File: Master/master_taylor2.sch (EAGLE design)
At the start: 43 parts, among them J1 ISP, K1 653002114822, K2 653002114822, K3 653002114822, K4 653002114822, U1 ATMEGA128RFA1, U2 TPS73633-DBVT, U3 ULN2003ADR, Y1 16MHz

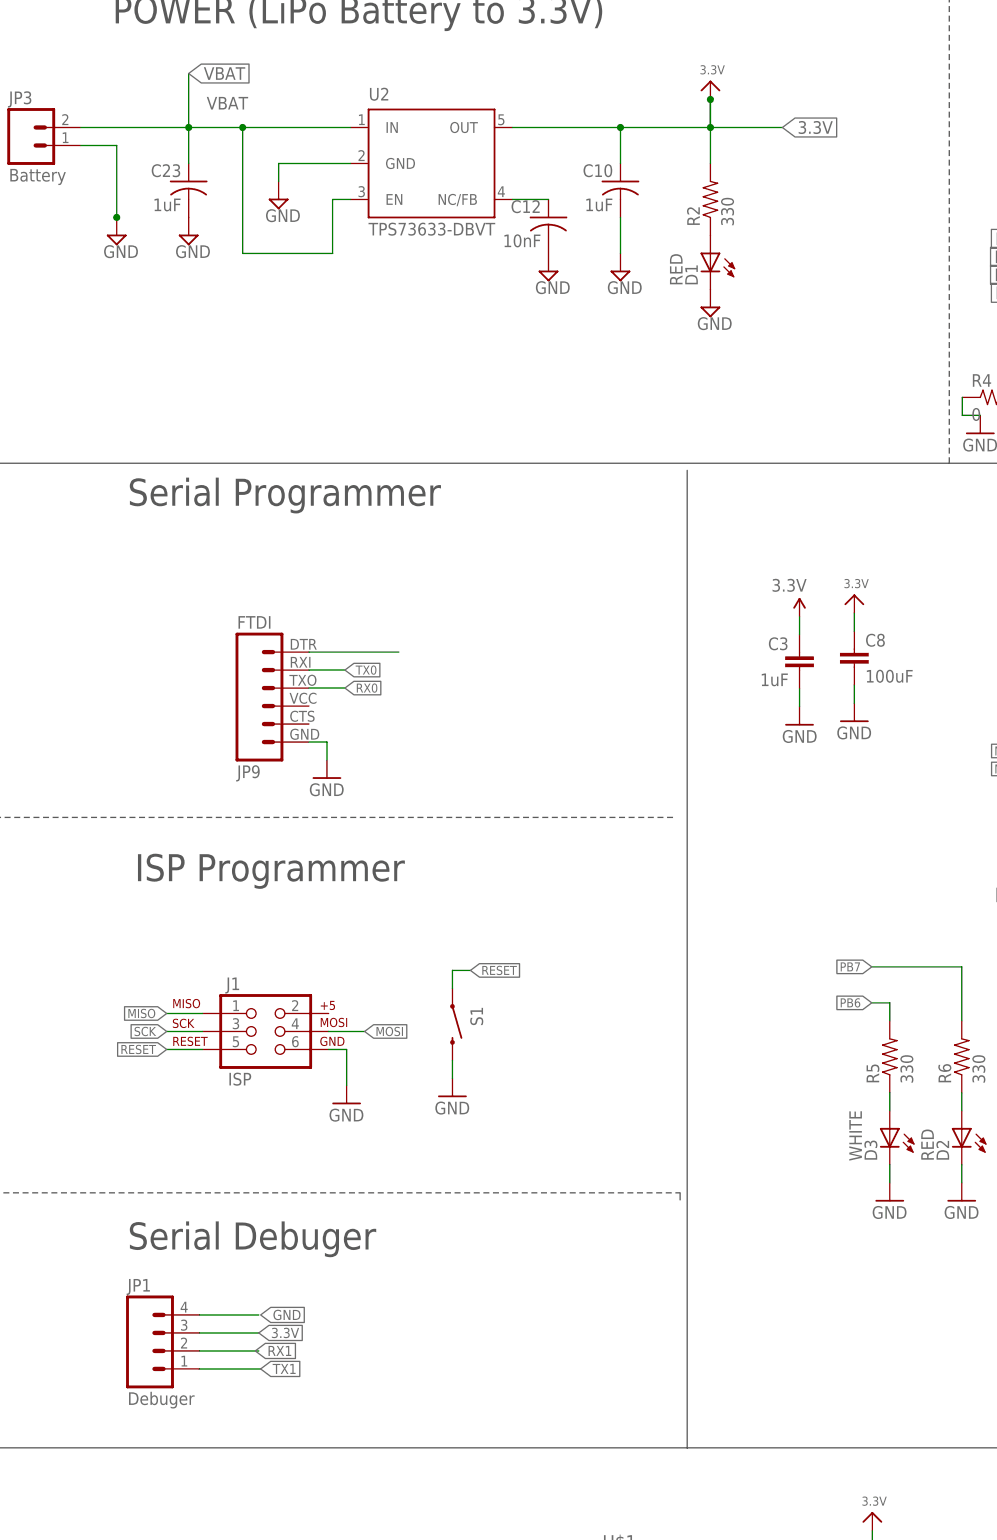
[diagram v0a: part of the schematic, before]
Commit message: Version 2 routed
Layed out crystal and antenna in accordance with the Cult of Sparkfun
Added keepouts to IMU because of Jorge's recommendation
Added keepout to antenna to not disturb the ether wind.
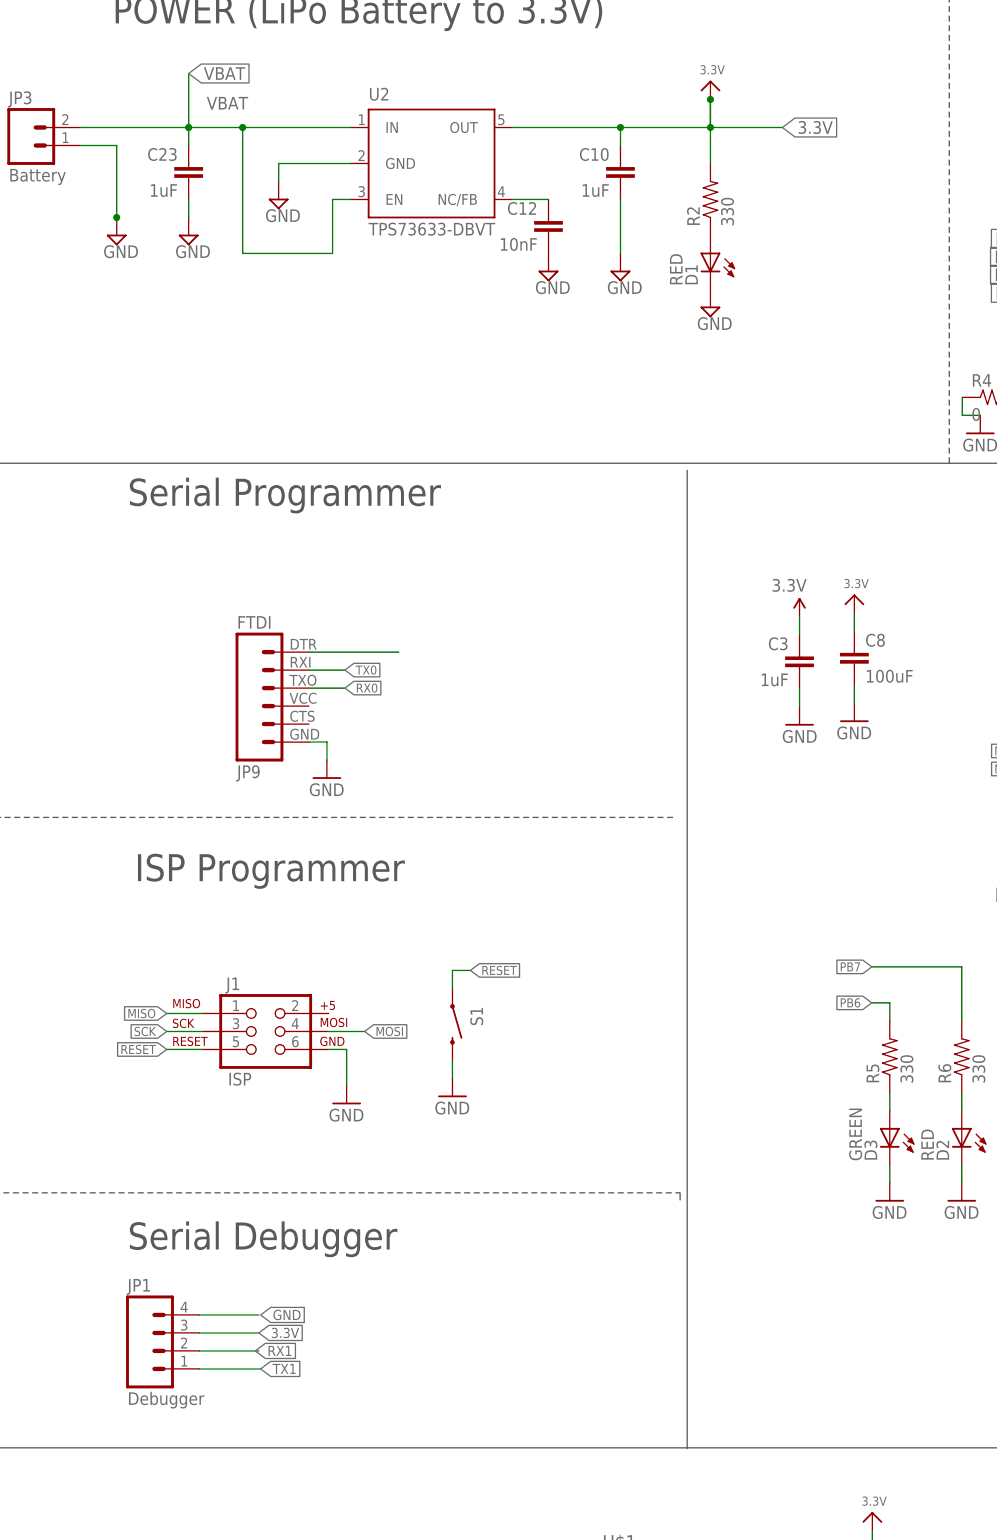
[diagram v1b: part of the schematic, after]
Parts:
- C10, C12, C23: device resistor:C-USC0805 -> SparkFun-Capacitors:CAP0603-CAP
- D3: value WHITE -> GREEN
- JP1: value Debuger -> Debugger
- U1: device SparkFun-DigitalIC:ATMEGA128RFA1 -> master_devon:ATMEGA128RFA1
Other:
- note added: "Serial Debugger"
- note removed: "Serial Debuger"
- moved on the sheet: C10, C23
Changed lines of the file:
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@@
 </classes>
 <parts>
-<part name="U1" library="SparkFun-DigitalIC" deviceset="ATMEGA128RFA1" device=""/>
+<part name="U1" library="master_devon" deviceset="ATMEGA128RFA1" device=""/>
 <part name="GND1" library="SparkFun-Aesthetics" deviceset="GND" device=""/>
 <part name="C1" library="SparkFun-Capacitors" deviceset="CAP" device="0603-CAP" value="1uF"/>
@@
 <part name="C6" library="SparkFun-Capacitors" deviceset="CAP" device="0603-CAP" value="12pF"/>
 <part name="GND6" library="SparkFun-Aesthetics" deviceset="GND" device=""/>
-<part name="GND7" library="SparkFun-Aesthetics" deviceset="GND" device=""/>
+<part name="GND7INF" library="SparkFun-Aesthetics" deviceset="GND" device=""/>
 <part name="B1" library="SparkFun-RF" deviceset="BALUN" device="0805" value="748421245"/>
 <part name="C11" library="SparkFun-Capacitors" deviceset="CAP" device="0603-CAP" value="22pF"/>
@@
 <part name="C16" library="SparkFun-Capacitors" deviceset="CAP" device="0603-CAP" value="JUMP"/>
 <part name="C17" library="SparkFun-Capacitors" deviceset="CAP" device="0603-CAP" value="JUMP"/>
-<part name="D3" library="led" deviceset="LED" device="CHIPLED_0603" value="WHITE"/>
+<part name="D3" library="led" deviceset="LED" device="CHIPLED_0603" value="GREEN"/>
 <part name="R5" library="SparkFun-Resistors" deviceset="RESISTOR" device="0603-RES" value="330"/>
 <part name="R6" library="SparkFun-Resistors" deviceset="RESISTOR" device="0603-RES" value="330"/>
@@
 <part name="SUPPLY8" library="supply2" deviceset="GND" device=""/>
 <part name="U2" library="Power" deviceset="TPS73633-DBVT" device=""/>
-<part name="C10" library="resistor" deviceset="C-US" device="C0805" value="1uF"/>
+<part name="C10" library="SparkFun-Capacitors" deviceset="CAP" device="0603-CAP" value="1uF"/>
 <part name="SUPPLY2" library="supply2" deviceset="GND" device=""/>
-<part name="C12" library="resistor" deviceset="C-US" device="C0805" value="10nF"/>
-<part name="C23" library="resistor" deviceset="C-US" device="C0805" value="1uF"/>
+<part name="C12" library="SparkFun-Capacitors" deviceset="CAP" device="0603-CAP" value="10nF"/>
+<part name="C23" library="SparkFun-Capacitors" deviceset="CAP" device="0603-CAP" value="1uF"/>
 <part name="SUPPLY3" library="supply2" deviceset="GND" device=""/>
 <part name="R2" library="SparkFun-Resistors" deviceset="RESISTOR" device="0603-RES" value="330"/>
@@
 <part name="SUPPLY4" library="supply2" deviceset="GND" device=""/>
 <part name="FRAME1" library="frames" deviceset="FRAME_B_L" device="" value="NONE"/>
-<part name="JP1" library="SparkFun-Connectors" deviceset="M04" device="PTH" value="Debuger"/>
+<part name="JP1" library="SparkFun-Connectors" deviceset="M04" device="PTH" value="Debugger"/>
 <part name="U$2" library="microbuilder" deviceset="3.3V" device=""/>
 <part name="U$1" library="IMU_parts" deviceset="LSM9DS0" device=""/>
@@
 <text x="-255" y="226" size="3.81" layer="97">Serial Programmer</text>
 <text x="-254" y="173" size="3.81" layer="97">ISP Programmer</text>
-<text x="-255" y="121" size="3.81" layer="97">Serial Debuger</text>
+<text x="-255" y="121" size="3.81" layer="97">Serial Debugger</text>
 <text x="-123" y="220" size="3.81" layer="97">ATMEL RF Microcontroller </text>
 <wire x1="38.354" y1="66.294" x2="38.354" y2="232.156" width="0.1524" layer="97"/>
@@
 </instance>
 <instance part="GND6" gate="1" x="-40.72" y="138.04" rot="MR0"/>
-<instance part="GND7" gate="1" x="-50.88" y="138.04" rot="MR0"/>
+<instance part="GND7INF" gate="1" x="-50.88" y="138.04" rot="MR0"/>
 <instance part="B1" gate="G$1" x="-15.32" y="183.76" smashed="yes" rot="MR0">
 <attribute name="VALUE" x="-10.24" y="174.108" size="1.778" layer="96" rot="MR90"/>
@@
 <instance part="C10" gate="G$1" x="-185.42" y="271.78" rot="MR0"/>
 <instance part="SUPPLY2" gate="GND" x="-185.42" y="259.08"/>
-<instance part="C12" gate="G$1" x="-195.58" y="266.7" rot="MR0"/>
+<instance part="C12" gate="G$1" x="-195.58" y="264.16" rot="MR0"/>
 <instance part="C23" gate="G$1" x="-246.38" y="271.78" rot="MR0"/>
 <instance part="SUPPLY3" gate="GND" x="-233.68" y="269.24"/>
@@
 <segment>
 <pinref part="C6" gate="G$1" pin="2"/>
-<pinref part="GND7" gate="1" pin="GND"/>
+<pinref part="GND7INF" gate="1" pin="GND"/>
 <wire x1="-50.88" y1="140.58" x2="-50.88" y2="143.12" width="0.1524" layer="91"/>
 </segment>
@@
 <pinref part="C10" gate="G$1" pin="2"/>
 <pinref part="SUPPLY2" gate="GND" pin="GND"/>
-<wire x1="-185.42" y1="266.7" x2="-185.42" y2="261.62" width="0.1524" layer="91"/>
+<wire x1="-185.42" y1="269.24" x2="-185.42" y2="261.62" width="0.1524" layer="91"/>
 </segment>
 <segment>
@@
 <pinref part="SUPPLY8" gate="GND" pin="GND"/>
 <pinref part="C23" gate="G$1" pin="2"/>
+<wire x1="-246.38" y1="266.7" x2="-246.38" y2="269.24" width="0.1524" layer="91"/>
 </segment>
 <segment>
@@
 <wire x1="-200.66" y1="279.4" x2="-185.42" y2="279.4" width="0.1524" layer="91"/>
 <pinref part="C10" gate="G$1" pin="1"/>
-<wire x1="-185.42" y1="274.32" x2="-185.42" y2="279.4" width="0.1524" layer="91"/>
+<wire x1="-185.42" y1="276.86" x2="-185.42" y2="279.4" width="0.1524" layer="91"/>
 <wire x1="-185.42" y1="279.4" x2="-172.72" y2="279.4" width="0.1524" layer="91"/>
 <label x="-162.56" y="279.4" size="1.778" layer="95" xref="yes"/>
@@
 <wire x1="-261.62" y1="279.4" x2="-246.38" y2="279.4" width="0.1524" layer="91"/>
 <pinref part="C23" gate="G$1" pin="1"/>
-<wire x1="-246.38" y1="274.32" x2="-246.38" y2="279.4" width="0.1524" layer="91"/>
+<wire x1="-246.38" y1="276.86" x2="-246.38" y2="279.4" width="0.1524" layer="91"/>
 <junction x="-246.38" y="279.4"/>
 <wire x1="-246.38" y1="279.4" x2="-238.76" y2="279.4" width="0.1524" layer="91"/>
@@
 </sheet>
 </sheets>
-<errors>
-</errors>
 </schematic>
 </drawing>

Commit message: ng
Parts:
- renumbered K1 to WING_BL, K2 to WING_BR, K3 to WING_FL, K4 to WING_FR
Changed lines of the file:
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@@
 <part name="GND31" library="SparkFun" deviceset="GND" device=""/>
 <part name="A1" library="SparkFun-RF" deviceset="ANTENNA2" device="SMD5"/>
-<part name="K1" library="Wuerth_Elektronik_eiCan_Wire_to_Board_Connectors" deviceset="653002114822" device="">
+<part name="WING_BL" library="Wuerth_Elektronik_eiCan_Wire_to_Board_Connectors" deviceset="653002114822" device="">
 <attribute name="MF" value=""/>
 <attribute name="MPN" value=""/>
 <attribute name="OC_FARNELL" value="unknown"/>
 </part>
-<part name="K2" library="Wuerth_Elektronik_eiCan_Wire_to_Board_Connectors" deviceset="653002114822" device="">
+<part name="WING_BR" library="Wuerth_Elektronik_eiCan_Wire_to_Board_Connectors" deviceset="653002114822" device="">
 <attribute name="MF" value=""/>
 <attribute name="MPN" value=""/>
 <attribute name="OC_FARNELL" value="unknown"/>
 </part>
-<part name="K3" library="Wuerth_Elektronik_eiCan_Wire_to_Board_Connectors" deviceset="653002114822" device="">
+<part name="WING_FL" library="Wuerth_Elektronik_eiCan_Wire_to_Board_Connectors" deviceset="653002114822" device="">
 <attribute name="MF" value=""/>
 <attribute name="MPN" value=""/>
 <attribute name="OC_FARNELL" value="unknown"/>
 </part>
-<part name="K4" library="Wuerth_Elektronik_eiCan_Wire_to_Board_Connectors" deviceset="653002114822" device="">
+<part name="WING_FR" library="Wuerth_Elektronik_eiCan_Wire_to_Board_Connectors" deviceset="653002114822" device="">
 <attribute name="MF" value=""/>
 <attribute name="MPN" value=""/>
@@
 <instance part="GND31" gate="1" x="-137.24" y="127.88"/>
 <instance part="A1" gate="G$1" x="2.46" y="199"/>
-<instance part="K1" gate="G$1" x="-88.18" y="275.16" rot="R90">
+<instance part="WING_BL" gate="G$1" x="-88.18" y="275.16" rot="R90">
 <attribute name="OC_FARNELL" x="-88.18" y="275.16" size="1.778" layer="96" display="off"/>
 <attribute name="MF" x="-88.18" y="275.16" size="1.778" layer="96" display="off"/>
 <attribute name="MPN" x="-88.18" y="275.16" size="1.778" layer="96" display="off"/>
 </instance>
-<instance part="K2" gate="G$1" x="-62.78" y="275.16" rot="R90">
+<instance part="WING_BR" gate="G$1" x="-62.78" y="275.16" rot="R90">
 <attribute name="OC_FARNELL" x="-62.78" y="275.16" size="1.778" layer="96" display="off"/>
 <attribute name="MF" x="-62.78" y="275.16" size="1.778" layer="96" display="off"/>
 <attribute name="MPN" x="-62.78" y="275.16" size="1.778" layer="96" display="off"/>
 </instance>
-<instance part="K3" gate="G$1" x="-37.38" y="275.16" rot="R90">
+<instance part="WING_FL" gate="G$1" x="-37.38" y="275.16" rot="R90">
 <attribute name="OC_FARNELL" x="-37.38" y="275.16" size="1.778" layer="96" display="off"/>
 <attribute name="MF" x="-37.38" y="275.16" size="1.778" layer="96" display="off"/>
 <attribute name="MPN" x="-37.38" y="275.16" size="1.778" layer="96" display="off"/>
 </instance>
-<instance part="K4" gate="G$1" x="-11.98" y="275.16" rot="R90">
+<instance part="WING_FR" gate="G$1" x="-11.98" y="275.16" rot="R90">
 <attribute name="OC_FARNELL" x="-11.98" y="275.16" size="1.778" layer="96" display="off"/>
 <attribute name="MF" x="-11.98" y="275.16" size="1.778" layer="96" display="off"/>
@@
 <wire x1="-88.9" y1="264.16" x2="-75.48" y2="263.68" width="0.1524" layer="91"/>
 <wire x1="-75.48" y1="263.68" x2="-75.48" y2="272.62" width="0.1524" layer="91"/>
-<pinref part="K1" gate="G$1" pin="2"/>
+<pinref part="WING_BL" gate="G$1" pin="2"/>
 <wire x1="-75.48" y1="272.62" x2="-80.56" y2="272.62" width="0.1524" layer="91"/>
 </segment>
@@
 <segment>
 <pinref part="U3" gate="A" pin="2C"/>
-<pinref part="K2" gate="G$1" pin="2"/>
+<pinref part="WING_BR" gate="G$1" pin="2"/>
 <wire x1="-88.9" y1="261.62" x2="-55.16" y2="261.14" width="0.1524" layer="91"/>
 <wire x1="-55.16" y1="261.14" x2="-55.16" y2="272.62" width="0.1524" layer="91"/>
@@
 <wire x1="-88.9" y1="259.08" x2="-27.22" y2="258.6" width="0.1524" layer="91"/>
 <wire x1="-27.22" y1="258.6" x2="-27.22" y2="272.62" width="0.1524" layer="91"/>
-<pinref part="K3" gate="G$1" pin="2"/>
+<pinref part="WING_FL" gate="G$1" pin="2"/>
 <wire x1="-27.22" y1="272.62" x2="-29.76" y2="272.62" width="0.1524" layer="91"/>
 </segment>
@@
 <wire x1="-88.9" y1="256.54" x2="-1.82" y2="256.06" width="0.1524" layer="91"/>
 <wire x1="-1.82" y1="256.06" x2="-1.82" y2="272.62" width="0.1524" layer="91"/>
-<pinref part="K4" gate="G$1" pin="2"/>
+<pinref part="WING_FR" gate="G$1" pin="2"/>
 <wire x1="-1.82" y1="272.62" x2="-4.36" y2="272.62" width="0.1524" layer="91"/>
 </segment>
@@
 <wire x1="-52.62" y1="292.94" x2="-78.02" y2="292.94" width="0.1524" layer="91"/>
 <wire x1="-78.02" y1="292.94" x2="-78.02" y2="277.7" width="0.1524" layer="91"/>
-<pinref part="K1" gate="G$1" pin="1"/>
+<pinref part="WING_BL" gate="G$1" pin="1"/>
 <wire x1="-78.02" y1="277.7" x2="-80.56" y2="277.7" width="0.1524" layer="91"/>
-<pinref part="K2" gate="G$1" pin="1"/>
+<pinref part="WING_BR" gate="G$1" pin="1"/>
 <wire x1="-55.16" y1="277.7" x2="-52.62" y2="277.7" width="0.1524" layer="91"/>
 <wire x1="-52.62" y1="277.7" x2="-52.62" y2="292.94" width="0.1524" layer="91"/>
-<pinref part="K3" gate="G$1" pin="1"/>
+<pinref part="WING_FL" gate="G$1" pin="1"/>
 <wire x1="-29.76" y1="277.7" x2="-27.22" y2="277.7" width="0.1524" layer="91"/>
 <wire x1="-27.22" y1="277.7" x2="-27.22" y2="292.94" width="0.1524" layer="91"/>
 <wire x1="-1.82" y1="277.7" x2="-1.82" y2="292.94" width="0.1524" layer="91"/>
-<pinref part="K4" gate="G$1" pin="1"/>
+<pinref part="WING_FR" gate="G$1" pin="1"/>
 <wire x1="-4.36" y1="277.7" x2="-1.82" y2="277.7" width="0.1524" layer="91"/>
 <junction x="-27.22" y="292.94"/>
